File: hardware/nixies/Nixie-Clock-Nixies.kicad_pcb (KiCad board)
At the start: 2 copper layers, 228.6 x 52.1 mm, 25 parts, among them J1 Nixies-Connector

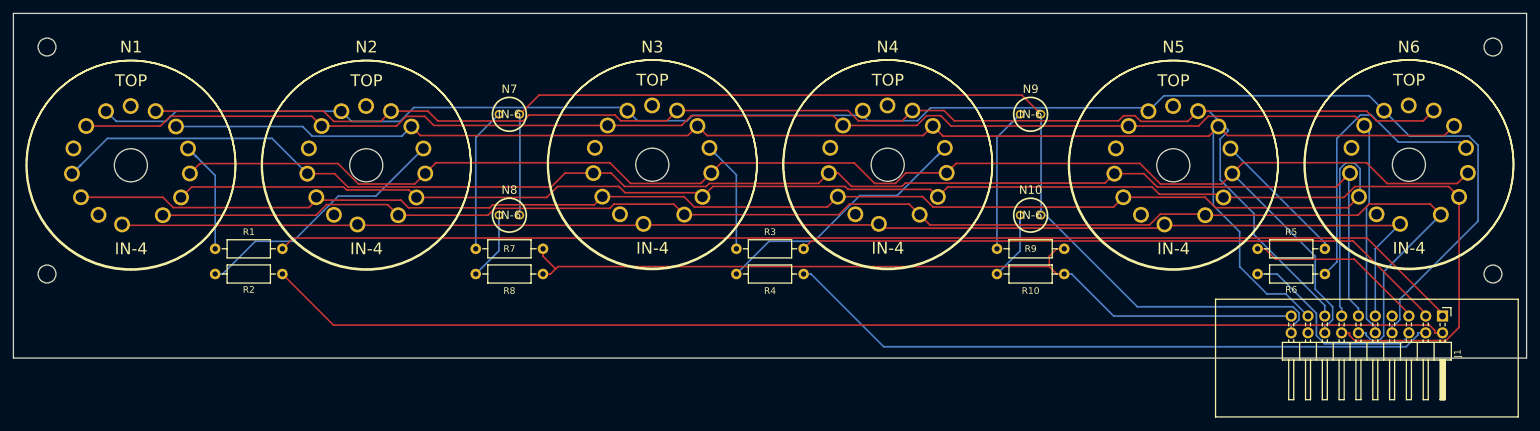
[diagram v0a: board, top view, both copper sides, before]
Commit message: Change Mountingholes to M3
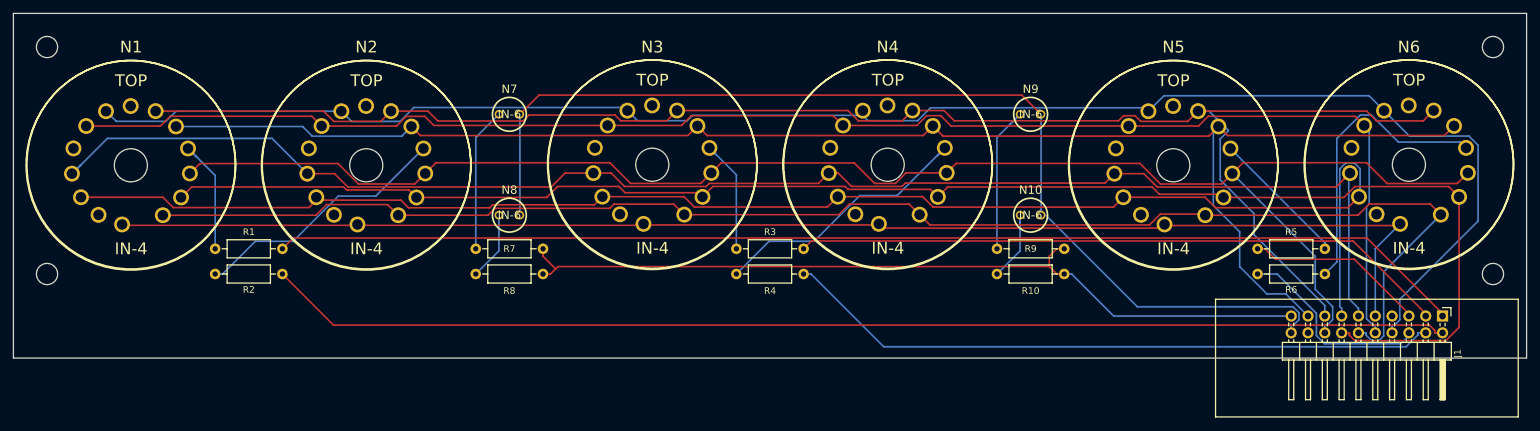
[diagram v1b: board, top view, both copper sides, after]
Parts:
- H1, H2, H3, H4: footprint MountingHole:MountingHole_2.7mm_M2.5 -> MountingHole:MountingHole_3.2mm_M3

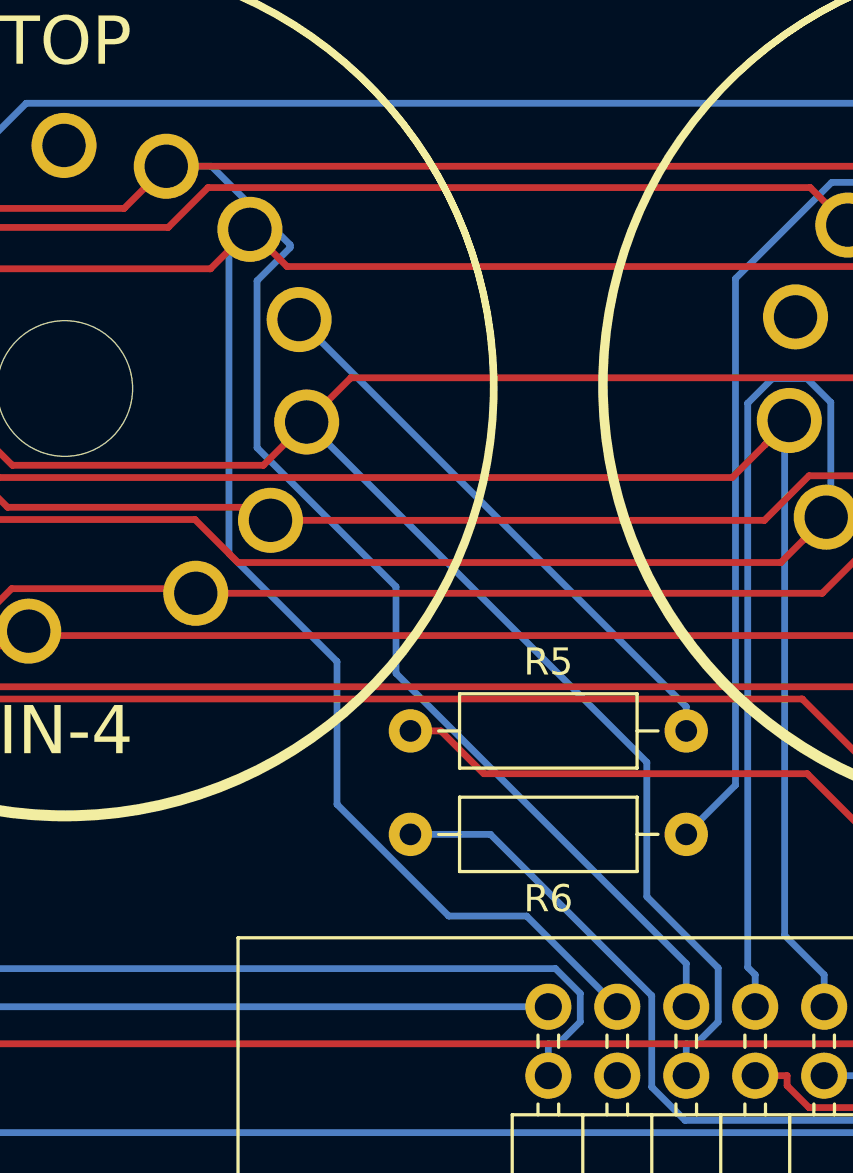
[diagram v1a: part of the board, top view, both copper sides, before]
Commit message: Fix path error
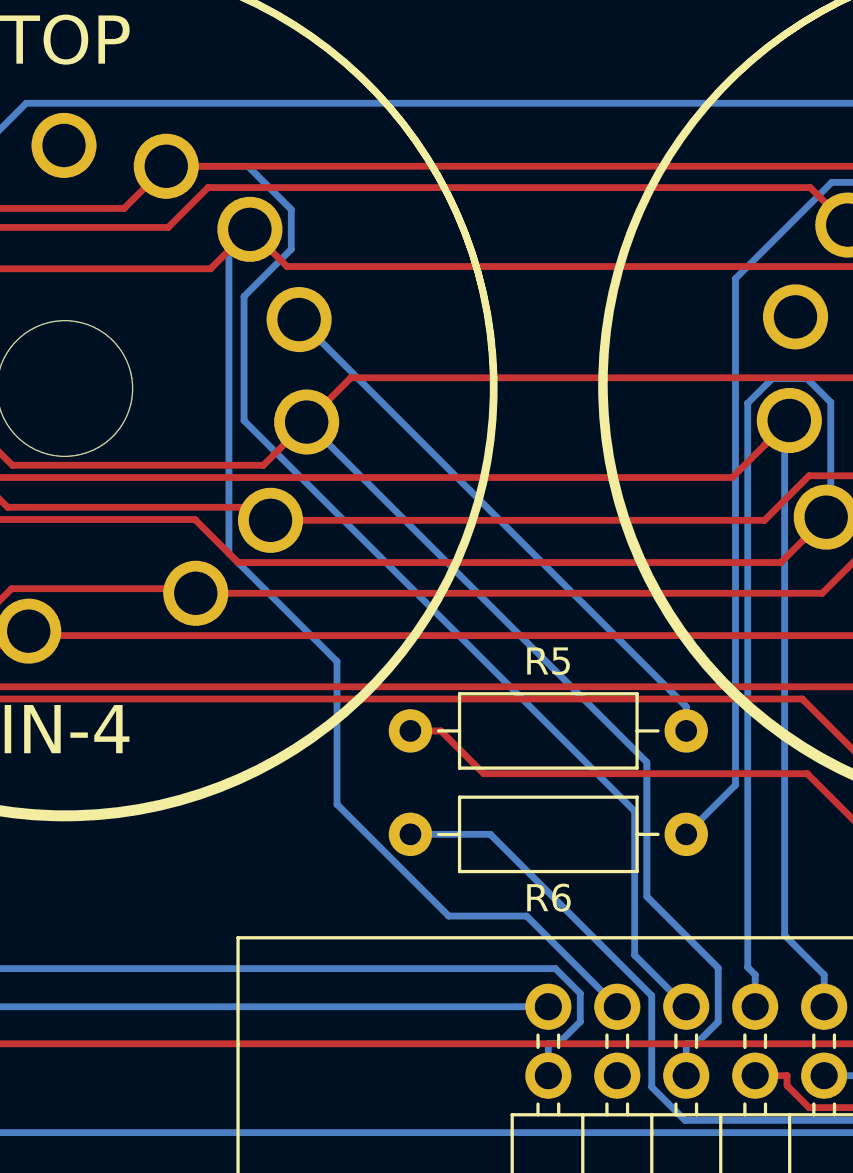
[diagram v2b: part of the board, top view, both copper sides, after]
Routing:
- net /c7: track 241.7 -> 243.0 mm
